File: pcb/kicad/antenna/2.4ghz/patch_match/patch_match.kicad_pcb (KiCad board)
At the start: 2 copper layers, 19 parts, among them P1 SMA

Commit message: Cleanup balun patch to match regular patch antenna
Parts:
- removed the REF** at (146.5, 112.3)
- removed the REF** at (146.5, 115.8)
- removed the REF** at (146.5, 115.0)
- removed the REF** at (146.5, 118.5)
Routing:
- net GND: vias 0 -> 4
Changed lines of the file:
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@@
 (kicad_pcb (version 4) (host pcbnew 4.0.5)
   (general
-    (links 28)
+    (links 24)
     (no_connects 0)
     (area 123.063 64.376 272.295714 194.39)
     (thickness 1.6)
     (drawings 7)
-    (tracks 18)
+    (tracks 22)
     (zones 0)
-    (modules 19)
+    (modules 15)
     (nets 6)
   )
@@
     (visible_elements 7FFEFF7F)
     (pcbplotparams
-      (layerselection 0x000f0_80000001)
+      (layerselection 0x020f0_80000001)
       (usegerberextensions false)
       (excludeedgelayer true)
@@
       (net 1 GND) (zone_connect 2))
   )
-  (module Misc:Via_Stitch_Dia0.508mm_Drill0.254mm (layer F.Cu)
-    (at 146.5072 112.2934)
-    (fp_text reference REF** (at 0 0.889) (layer F.SilkS) hide
-      (effects (font (size 1 1) (thickness 0.15)))
-    )
-    (fp_text value Via_Stitch_Dia0.508mm_Drill0.254mm (at 0 -0.889) (layer F.Fab)
-      (effects (font (size 1 1) (thickness 0.15)))
-    )
-    (pad 1 thru_hole circle (at 0 0) (size 0.508 0.508) (drill 0.254) (layers *.Cu)
-      (net 1 GND) (zone_connect 2))
-  )
-  (module Misc:Via_Stitch_Dia0.508mm_Drill0.254mm (layer F.Cu)
-    (at 146.5072 115.7732)
-    (fp_text reference REF** (at 0 0.889) (layer F.SilkS) hide
-      (effects (font (size 1 1) (thickness 0.15)))
-    )
-    (fp_text value Via_Stitch_Dia0.508mm_Drill0.254mm (at 0 -0.889) (layer F.Fab)
-      (effects (font (size 1 1) (thickness 0.15)))
-    )
-    (pad 1 thru_hole circle (at 0 0) (size 0.508 0.508) (drill 0.254) (layers *.Cu)
-      (net 1 GND) (zone_connect 2))
-  )
-  (module Misc:Via_Stitch_Dia0.508mm_Drill0.254mm (layer F.Cu)
-    (at 146.5072 115.0112)
-    (fp_text reference REF** (at 0 0.889) (layer F.SilkS) hide
-      (effects (font (size 1 1) (thickness 0.15)))
-    )
-    (fp_text value Via_Stitch_Dia0.508mm_Drill0.254mm (at 0 -0.889) (layer F.Fab)
-      (effects (font (size 1 1) (thickness 0.15)))
-    )
-    (pad 1 thru_hole circle (at 0 0) (size 0.508 0.508) (drill 0.254) (layers *.Cu)
-      (net 1 GND) (zone_connect 2))
-  )
-  (module Misc:Via_Stitch_Dia0.508mm_Drill0.254mm (layer F.Cu)
-    (at 146.5072 118.491)
-    (fp_text reference REF** (at 0 0.889) (layer F.SilkS) hide
-      (effects (font (size 1 1) (thickness 0.15)))
-    )
-    (fp_text value Via_Stitch_Dia0.508mm_Drill0.254mm (at 0 -0.889) (layer F.Fab)
-      (effects (font (size 1 1) (thickness 0.15)))
-    )
-    (pad 1 thru_hole circle (at 0 0) (size 0.508 0.508) (drill 0.254) (layers *.Cu)
-      (net 1 GND) (zone_connect 2))
-  )
   (module Misc:Via_Stitch_Dia0.356mm_Drill0.254mm (layer F.Cu)
     (at 146.3294 113.1062)
@@
     (effects (font (size 1.5 1.5) (thickness 0.3)))
   )
-  (segment (start 146.2063 112.2934) (end 146.5072 112.2934) (width 0.508) (layer F.Cu) (net 1))
-  (segment (start 146.2063 118.491) (end 146.5072 118.491) (width 0.508) (layer F.Cu) (net 1))
+  (segment (start 146.2063 112.2934) (end 146.5072 112.2934) (width 0.508) (layer F.Cu) (net 1) (status 400000))
+  (via (at 146.5072 112.2934) (size 0.508) (drill 0.254) (layers F.Cu B.Cu) (net 1))
+  (segment (start 146.2063 118.491) (end 146.5072 118.491) (width 0.508) (layer F.Cu) (net 1) (status 400000))
+  (via (at 146.5072 118.491) (size 0.508) (drill 0.254) (layers F.Cu B.Cu) (net 1))
   (segment (start 146.2063 115.7732) (end 146.5072 115.7732) (width 0.508) (layer F.Cu) (net 1))
+  (via (at 146.5072 115.7732) (size 0.508) (drill 0.254) (layers F.Cu B.Cu) (net 1))
   (segment (start 146.2063 115.0112) (end 146.5072 115.0112) (width 0.508) (layer F.Cu) (net 1))
+  (via (at 146.5072 115.0112) (size 0.508) (drill 0.254) (layers F.Cu B.Cu) (net 1))
   (segment (start 145.1063 112.2934) (end 145.1063 92.3837) (width 0.508) (layer F.Cu) (net 2))
   (segment (start 145.1063 92.3837) (end 148.59 88.9) (width 0.508) (layer F.Cu) (net 2))

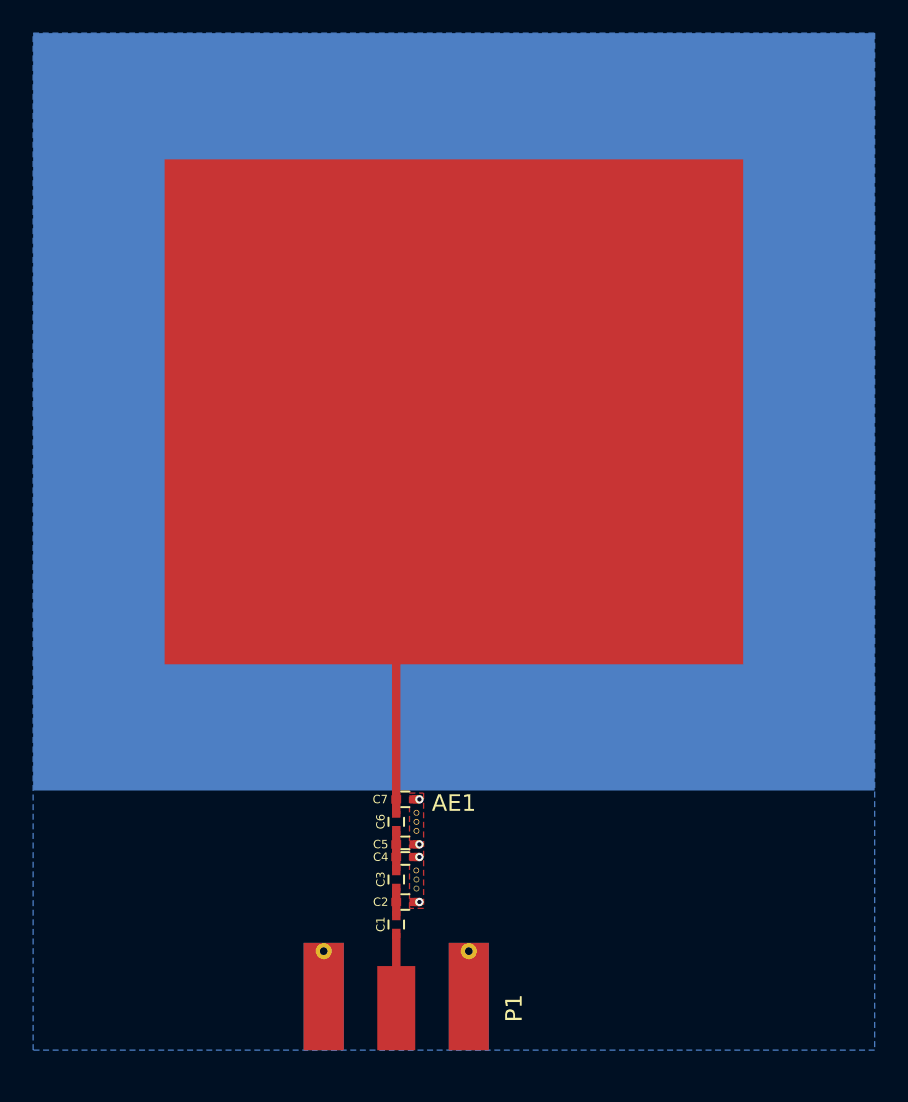
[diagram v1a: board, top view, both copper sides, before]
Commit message: Add patch antennas with transmission line matching
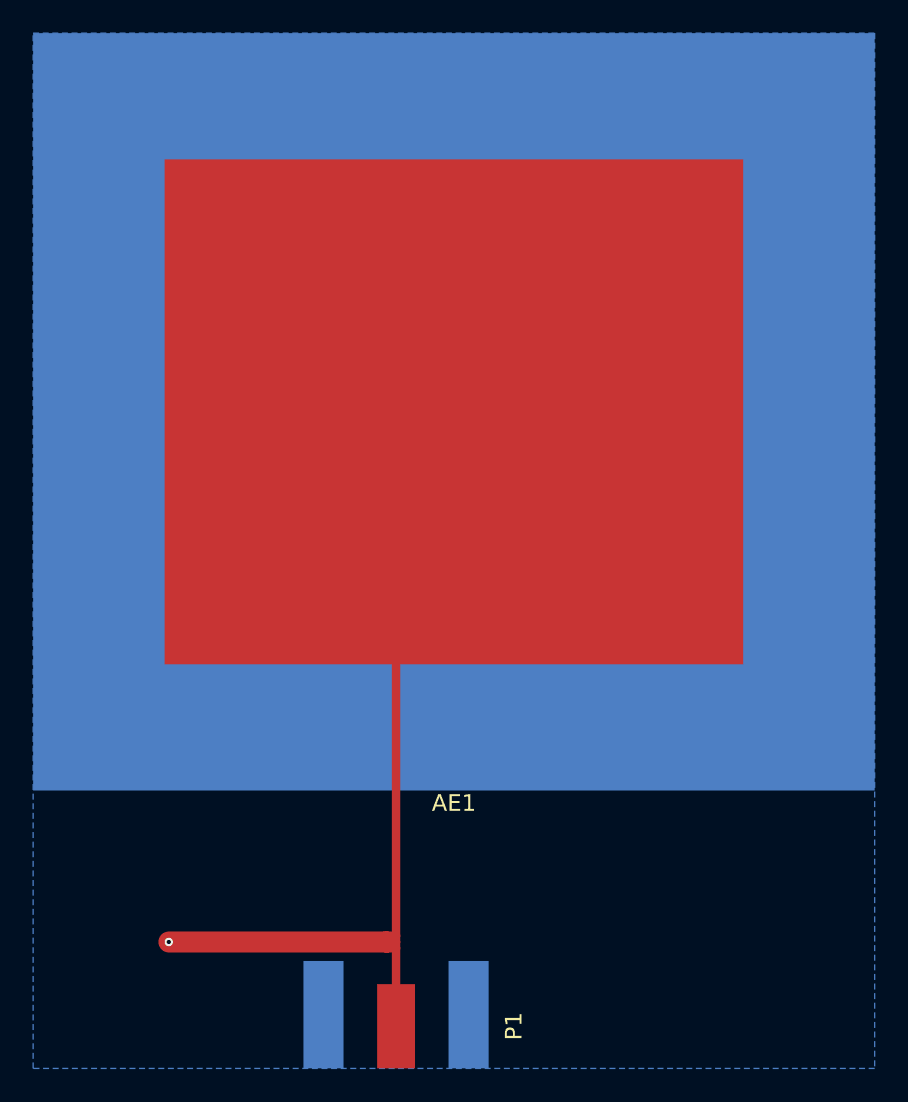
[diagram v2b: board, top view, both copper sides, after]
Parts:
- removed C1, C2, C3, C4, C5, C6, C7: C_Small, Capacitors_SMD:C_0402
- removed REF** (x6): Via_Stitch_Dia0.356mm_Drill0.254mm, Misc:Via_Stitch_Dia0.356mm_Drill0.254mm
- moved P1 1.09 mm to (145.1, 124.3)
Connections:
- AE1 pad 1: /SIG -> GND
- P1 pad 1: Net-(C1-Pad1) -> GND
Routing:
- net GND: track 1.20 -> 54.1 mm, vias 4 -> 1
- net /SIG: track 25.6 -> 0.00 mm
- net Net-(C1-Pad1): track 4.50 -> 0.00 mm
- net Net-(C3-Pad2): track 2.38 -> 0.00 mm
- net Net-(C1-Pad2): track 1.62 -> 0.00 mm
- removed copper zone on F.Cu, net GND
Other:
- rule pad_to_mask_clearance: 0.2 -> 0.0762
- board text added: "0.2"
- board text added: "April 28, 2017"
- board text removed: "0.1"
- board text removed: "April 4, 2017"

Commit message: Add new dimensions for base station
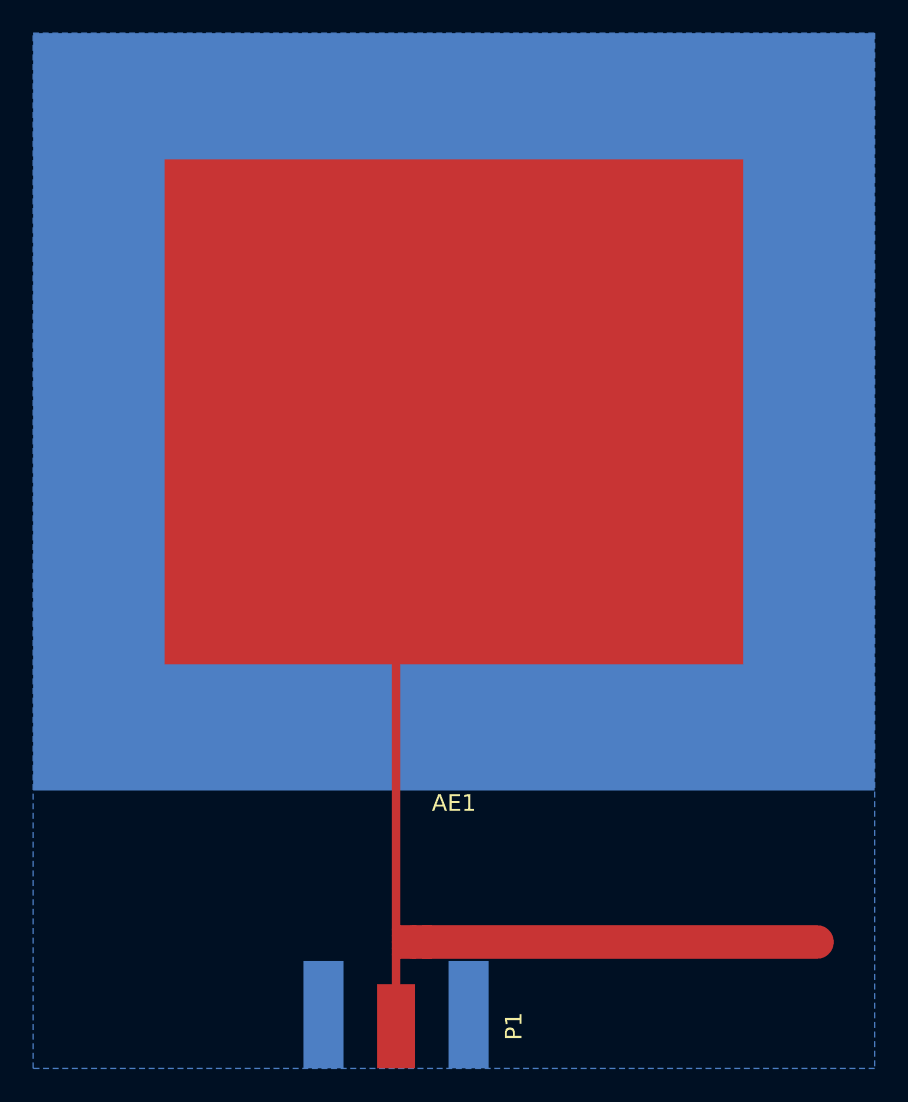
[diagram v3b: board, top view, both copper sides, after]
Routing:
- net GND: track 54.1 -> 68.3 mm, vias 1 -> 0
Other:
- board text added: "0.3"
- board text added: "June 1, 2017"
- board text removed: "0.2"
- board text removed: "April 28, 2017"
